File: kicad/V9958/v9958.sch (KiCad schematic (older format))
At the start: 21 parts, among them J1 Conn_01x01, J2 Conn_01x01, J3 Conn_01x04, J4 Conn_01x04, Q1 BC547, Q2 BC547, Q3 BC547, Q4 BC547, U1 7400, U2 V9958, Y1 21,443Mhz

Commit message: 4464 dram, preliminary schematic
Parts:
- added JP1: JUMPER, Pin_Headers:Pin_Header_Straight_1x02, symbol JUMPER
- added U3, U4, U5, U6: DRAM_64KX4, Housings_DIP:DIP-18_W7.62mm_LongPads, symbol DRAM_64KX4
- C1, C2: footprint (none) -> Capacitors_ThroughHole:C_Disc_D3_P2.5
- U1: footprint (none) -> Housings_DIP:DIP-14_W7.62mm_LongPads
- U2: footprint (none) -> Housings_DIP:DIP-64_W22.86mm_LongPads
- Y1: footprint (none) -> Crystals:Crystal_HC49-U_Vertical
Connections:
- net labels added: A0, A0..A7, A1, D0..D7, RD0..RD3, RD4..RD7, RDY
- wire segments 71 -> 114
- no-connect marks 0 -> 6
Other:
- moved on the sheet: J1, J2, J3, J4, Q1, Q2, Q3, Q4, R1, R2, R3, R4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

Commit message: cleanup, fixes
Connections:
- net labels added: /CAS0, /CAS1, /RAS, A2, A3, A4, A5, A6, A7, D0, D1, D2, D3, D4, D5, D6, D7, R/W, RD0, RD1, RD2, RD3, RD4, RD5, RD6, RD7
- wire segments 114 -> 180

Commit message: cxa stuff
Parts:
- removed J1, J2: Conn_01x01, Connect:1pin, symbol Conn_01x01
- removed J3, J4: Conn_01x04, Pin_Headers:Pin_Header_Straight_1x04_Pitch2.54mm, symbol Conn_01x04
- removed Q1, Q2, Q3, Q4: BC547, TO_SOT_Packages_THT:TO-92_Molded_Wide, symbol BC547
- added C10, C12, C13, C19, C3, C4, C5, C6, C7, C8, C9: 100n, Capacitors_ThroughHole:C_Disc_D3_P2.5, symbol C
- added C11, C17: 47µF, Capacitors_ThroughHole:C_Radial_D5_L11_P2.5, symbol CP
- added C14, C15, C16, C18, C20, C21: 220µF, Capacitors_ThroughHole:C_Radial_D6.3_L11.2_P2.5, symbol CP
- added R10: 2.61k/10%, Resistors_ThroughHole:R_Axial_DIN0207_L6.3mm_D2.5mm_P15.24mm_Horizontal, symbol R-RESCUE-v9958
- added R11, R12: 75, Resistors_ThroughHole:R_Axial_DIN0207_L6.3mm_D2.5mm_P15.24mm_Horizontal, symbol R-RESCUE-v9958
- added R13: 240, Resistors_ThroughHole:R_Axial_DIN0207_L6.3mm_D2.5mm_P15.24mm_Horizontal, symbol R-RESCUE-v9958
- added R9: 43, Resistors_ThroughHole:R_Axial_DIN0207_L6.3mm_D2.5mm_P15.24mm_Horizontal, symbol R-RESCUE-v9958
- added U7: cxa2075M, Housings_SOIC:SOIC-24_7.5x15.4mm_Pitch1.27mm, symbol cxa2075M
- added X1: OSC, Oscillators:KXO-200_LargePads, symbol OSC
- R1, R2, R3: value 1K -> 470
- R4: value 1K -> 2.2k
- R5: value 220 -> 2.2k
- R6, R7, R8: value 220 -> 75
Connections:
- net labels added: RD0..RD7
- net labels removed: RD0..RD3, RD4..RD7
- wire segments 180 -> 201
- no-connect marks 6 -> 8

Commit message: rca jacks, rough layout test
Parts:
- added P1, P2, P3, P4: RCA JACK, w_conn_av:rca_black, symbol CONN_01X02
- added X2: MINI_DIN_4, mini_din:mini_din-M_DIN4, symbol MINI_DIN_4
- R1, R10, R11, R12, R13, R2, R3, R4, R5, R6, R7, R8, R9: footprint Resistors_ThroughHole:R_Axial_DIN0207_L6.3mm_D2.5mm_P15.24mm_Horizontal -> Resistors_ThroughHole:Resistor_Horizontal_RM10mm
- U2: footprint Housings_DIP:DIP-64_W22.86mm_LongPads -> SDIP:SDIP64
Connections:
- net labels added: B_OUT, CV_OUT, C_OUT, G_OUT, R_OUT, Y_OUT
- wire segments 201 -> 221
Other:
- moved on the sheet: C3, C4, C5, C6, C7, C8

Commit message: cleanup
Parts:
- P1: value RCA JACK -> RED
- P2: value RCA JACK -> GREEN
- P3: value RCA JACK -> BLUE
- P4: value RCA JACK -> SYNC/C
- R1, R10, R11, R12, R13, R2, R3, R4, R5, R6, R7, R8, R9: footprint Resistors_ThroughHole:Resistor_Horizontal_RM10mm -> Discret:R3
- X2: value MINI_DIN_4 -> S-VIDEO
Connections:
- net labels added: AD0, AD1, AD2, AD3, AD4, AD5, AD6, AD7, VSS
- net labels removed: A2, A3, A4, A5, A6, A7
- wire segments 221 -> 231
- no-connect marks 8 -> 9
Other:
- moved on the sheet: C11, C13, C17, C19, R1, R2, R3, R4, R5

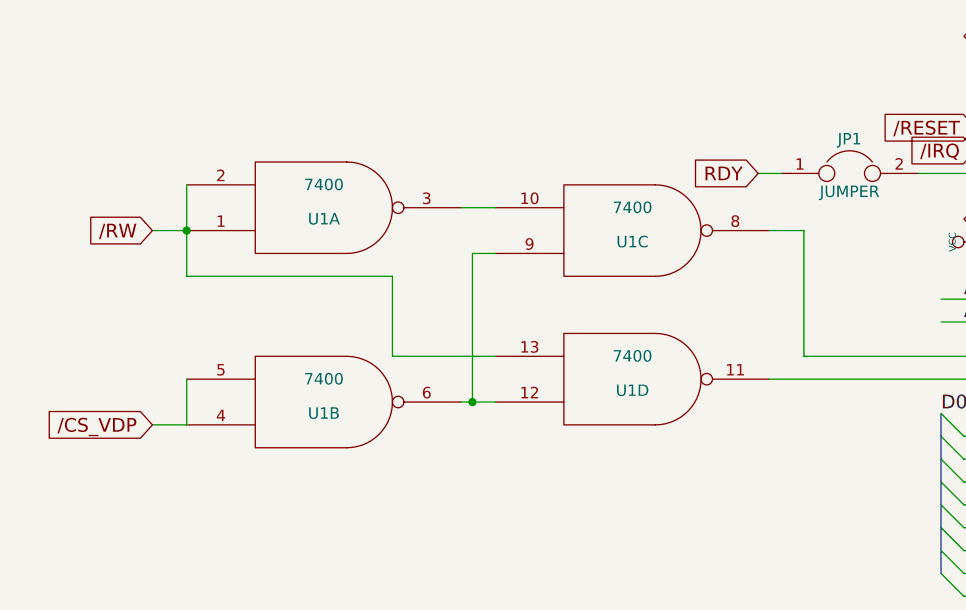
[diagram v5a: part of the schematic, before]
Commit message: 74139 instead of 7400
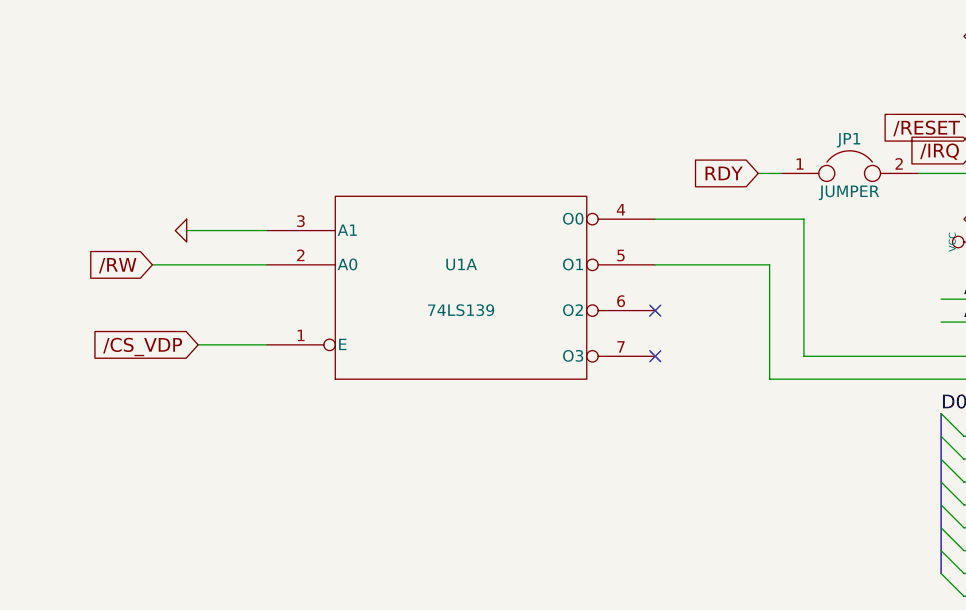
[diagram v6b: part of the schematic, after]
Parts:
- removed U1: 7400, Housings_DIP:DIP-14_W7.62mm_LongPads, symbol 7400
- added U1: 74LS139, Housings_DIP:DIP-16_W7.62mm_LongPads, symbol 74LS139
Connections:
- wire segments 231 -> 225
- no-connect marks 9 -> 11
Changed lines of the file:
@@
 Comment4 ""
 $EndDescr
-$Comp
-L 7400 U1
-U 2 1 5A27A3A8
-P 1700 2800
-F 0 "U1" H 1700 2850 50  0000 C CNN
-F 1 "7400" H 1700 2700 50  0000 C CNN
-F 2 "Housings_DIP:DIP-14_W7.62mm_LongPads" H 1700 2800 50  0001 C CNN
-F 3 "" H 1700 2800 50  0001 C CNN
-	2    1700 2800
-	1    0    0    1
-$EndComp
-$Comp
-L 7400 U1
-U 4 1 5A27A6C7
-P 3050 2700
-F 0 "U1" H 3050 2750 50  0000 C CNN
-F 1 "7400" H 3050 2600 50  0000 C CNN
-F 2 "Housings_DIP:DIP-14_W7.62mm_LongPads" H 3050 2700 50  0001 C CNN
-F 3 "" H 3050 2700 50  0001 C CNN
-	4    3050 2700
-	1    0    0    1
-$EndComp
-$Comp
-L 7400 U1
-U 1 1 5A27A724
-P 1700 1950
-F 0 "U1" H 1700 2000 50  0000 C CNN
-F 1 "7400" H 1700 1850 50  0000 C CNN
-F 2 "Housings_DIP:DIP-14_W7.62mm_LongPads" H 1700 1950 50  0001 C CNN
-F 3 "" H 1700 1950 50  0001 C CNN
-	1    1700 1950
-	1    0    0    1
-$EndComp
-$Comp
-L 7400 U1
-U 3 1 5A27A7E1
-P 3050 2050
-F 0 "U1" H 3050 2100 50  0000 C CNN
-F 1 "7400" H 3050 1950 50  0000 C CNN
-F 2 "Housings_DIP:DIP-14_W7.62mm_LongPads" H 3050 2050 50  0001 C CNN
-F 3 "" H 3050 2050 50  0001 C CNN
-	3    3050 2050
-	1    0    0    1
-$EndComp
-Text GLabel 950  2050 0    60   Input ~ 0
+Text GLabel 950  2200 0    60   Input ~ 0
 /RW
-Text GLabel 950  2900 0    60   Input ~ 0
+Text GLabel 1150 2550 0    60   Input ~ 0
 /CS_VDP
 $Comp
@@
 $EndComp
 Wire Wire Line
-	950  2900 1100 2900
-Wire Wire Line
-	2300 2800 2450 2800
-Connection ~ 1100 2050
-Wire Wire Line
-	2300 1950 2450 1950
-Wire Wire Line
-	2350 2150 2450 2150
-Wire Wire Line
-	2350 2150 2350 2800
-Connection ~ 2350 2800
-Wire Wire Line
-	2450 2600 2000 2600
-Wire Wire Line
-	2000 2600 2000 2250
-Wire Wire Line
-	2000 2250 1100 2250
-Wire Wire Line
-	1100 2250 1100 1850
-Wire Wire Line
-	1100 2900 1100 2700
-Wire Wire Line
-	1100 2050 950  2050
-Wire Wire Line
 	4550 3850 4700 3850
 Wire Wire Line
@@
 Wire Wire Line
 	4650 2600 3800 2600
-Wire Wire Line
-	3650 2050 3800 2050
-Wire Wire Line
-	3800 2050 3800 2600
 Wire Wire Line
 	4550 1700 4650 1700
@@
 Wire Wire Line
 	7150 4050 7150 5300
+$Comp
+L 74LS139 U1
+U 1 1 5A930A3D
+P 2300 2300
+F 0 "U1" H 2300 2400 50  0000 C CNN
+F 1 "74LS139" H 2300 2200 50  0000 C CNN
+F 2 "Housings_DIP:DIP-16_W7.62mm_LongPads" H 2300 2300 50  0001 C CNN
+F 3 "" H 2300 2300 50  0000 C CNN
+	1    2300 2300
+	1    0    0    -1
+$EndComp
+Wire Wire Line
+	1150 2550 1450 2550
+Wire Wire Line
+	950  2200 1450 2200
+$Comp
+L GND-RESCUE-v9958 #PWR031
+U 1 1 5A93119E
+P 1100 2050
+F 0 "#PWR031" H 1100 2050 30  0001 C CNN
+F 1 "GND" H 1100 1980 30  0001 C CNN
+F 2 "" H 1100 2050 60  0000 C CNN
+F 3 "" H 1100 2050 60  0000 C CNN
+	1    1100 2050
+	0    1    1    0
+$EndComp
+Wire Wire Line
+	1100 2050 1450 2050
+Wire Wire Line
+	3150 2000 3800 2000
+Wire Wire Line
+	3800 2000 3800 2600
+Wire Wire Line
+	3150 2200 3650 2200
+Wire Wire Line
+	3650 2200 3650 2700
+NoConn ~ 3150 2400
+NoConn ~ 3150 2600
 $EndSCHEMATC
